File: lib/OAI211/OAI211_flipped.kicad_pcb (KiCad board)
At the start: 2 copper layers, 8 parts

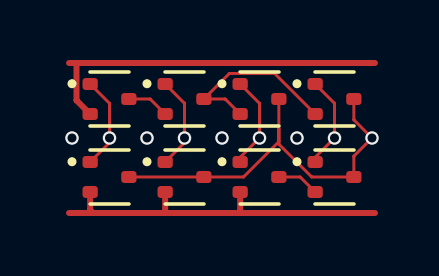
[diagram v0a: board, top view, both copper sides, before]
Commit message: High-density layout with pitch of 1.1mm, which gains 23% !!
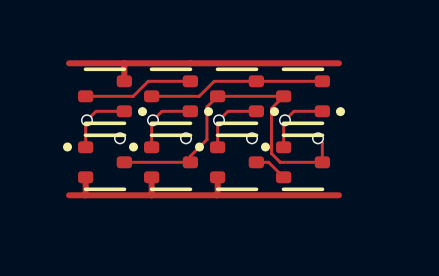
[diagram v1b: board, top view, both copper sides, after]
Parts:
- moved P4 1.16 mm to (7.70, 3.31)
- moved N4 1.05 mm to (7.70, 1.11), turned to 180 degrees
- moved P3 0.90 mm to (5.50, 3.31)
- moved N3 0.76 mm to (5.50, 1.11), turned to 180 degrees
- moved P2 0.67 mm to (3.30, 3.31)
- moved P1 0.51 mm to (1.10, 3.31)
- moved N2 0.46 mm to (3.30, 1.11), turned to 180 degrees
- moved N1 0.17 mm to (1.10, 1.11), turned to 180 degrees
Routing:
- net GND: track 12.1 -> 9.60 mm
- net intNA: track 1.42 -> 3.70 mm
- net Y: track 13.5 -> 11.7 mm
- net VDD: track 12.4 -> 10.8 mm
- net C1: track 3.13 -> 2.29 mm
- net A: track 3.13 -> 2.29 mm
- net B: track 3.13 -> 2.29 mm
- net C2: track 3.13 -> 2.29 mm
- net (no net): vias 4 -> 3

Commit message: All cells now use 1mm*4mm grid rather than 1.1mm*4.4mm
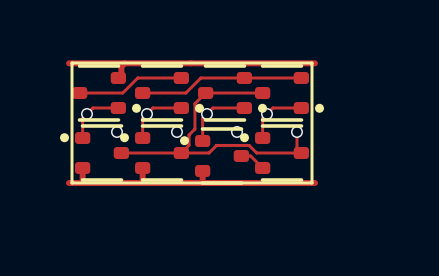
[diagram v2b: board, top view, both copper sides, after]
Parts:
- moved P4 0.77 mm to (7.00, 3.00)
- moved N4 0.71 mm to (7.00, 1.00)
- moved P3 0.54 mm to (5.00, 3.10)
- moved P2 0.43 mm to (3.00, 3.00)
- moved N3 0.41 mm to (5.10, 1.00)
- moved P1 0.33 mm to (1.00, 3.00)
- moved N2 0.32 mm to (3.00, 1.00)
- moved N1 0.23 mm to (0.90, 1.00)
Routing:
- net VDD: track 10.8 -> 9.76 mm
- net GND: track 9.60 -> 8.73 mm

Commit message: Make the pads of my SOT523 footprint very slightly smaller, which is enough to route all the cells and leave the mosfets exactly on the grid
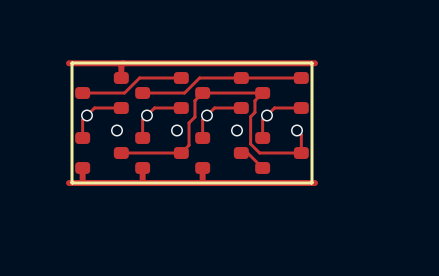
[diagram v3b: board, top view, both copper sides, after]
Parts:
- N1, N2, N3, N4, P1, P2, P3, P4: footprint Package_TO_SOT_SMD:SOT-523 -> RV523:SOT523
- moved P3 0.10 mm to (5.00, 3.00)
- moved N1 0.10 mm to (1.00, 1.00)
- moved N3 0.10 mm to (5.00, 1.00)
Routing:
- net Y: track 11.3 -> 10.8 mm

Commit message: Propagate MOSFET values to the cells' PCBs
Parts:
- N1, N2, N3, N4: value (none) -> NMOS
- P1, P2, P3, P4: value (none) -> PMOS
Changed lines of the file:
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@@
 			)
 		)
-		(property "Value" ""
+		(property "Value" "NMOS"
 			(at 0 0 180)
 			(layer "F.Fab")
@@
 			)
 		)
-		(property "Value" ""
+		(property "Value" "NMOS"
 			(at 0 0 180)
 			(layer "F.Fab")
@@
 			)
 		)
-		(property "Value" ""
+		(property "Value" "PMOS"
 			(at 0 0 0)
 			(layer "F.Fab")
@@
 			)
 		)
-		(property "Value" ""
+		(property "Value" "PMOS"
 			(at 0 0 0)
 			(layer "F.Fab")
@@
 			)
 		)
-		(property "Value" ""
+		(property "Value" "PMOS"
 			(at 0 0 0)
 			(layer "F.Fab")
@@
 			)
 		)
-		(property "Value" ""
+		(property "Value" "PMOS"
 			(at 0 0 0)
 			(layer "F.Fab")
@@
 			)
 		)
-		(property "Value" ""
+		(property "Value" "NMOS"
 			(at 0 0 180)
 			(layer "F.Fab")
@@
 			)
 		)
-		(property "Value" ""
+		(property "Value" "NMOS"
 			(at 0 0 180)
 			(layer "F.Fab")
